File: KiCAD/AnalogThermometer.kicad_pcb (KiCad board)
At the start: 2 copper layers, 26.7 x 25.4 mm, 19 parts, among them P1 Power, P2 uA, Q1 MMBT3904, U1 LTC1541, U2 MCP9700A, U3 MCP9700AT

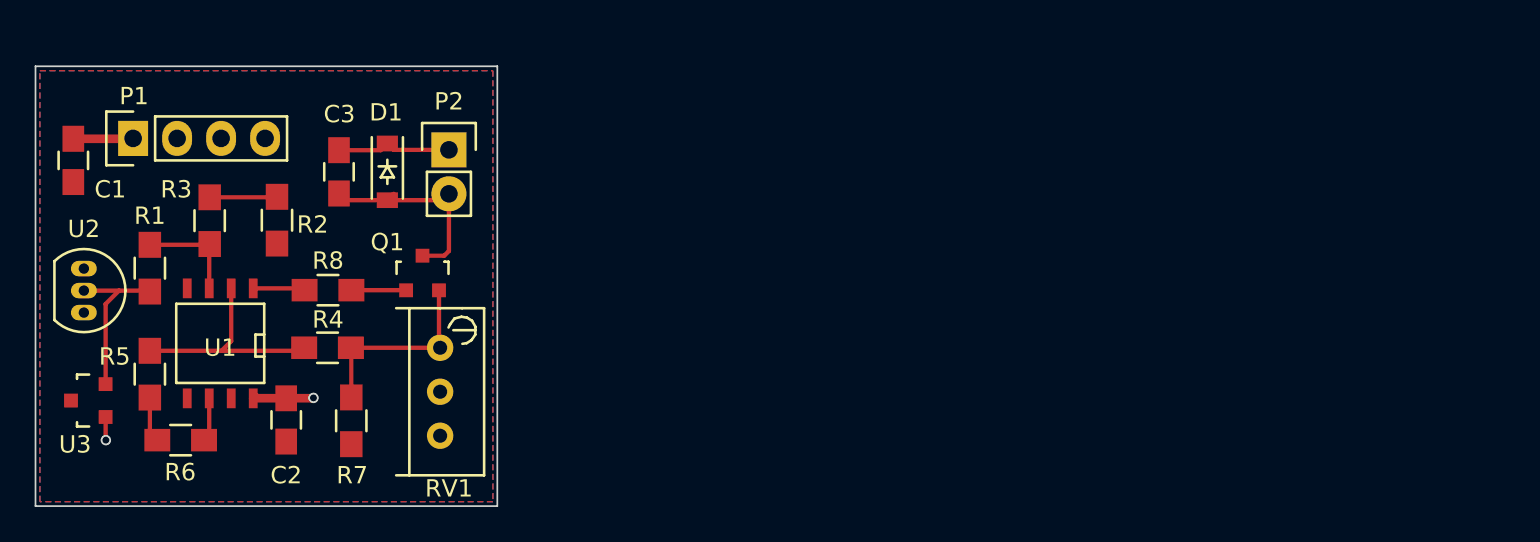
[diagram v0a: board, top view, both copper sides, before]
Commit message: Updated board and gerbers to be 1x1 inch
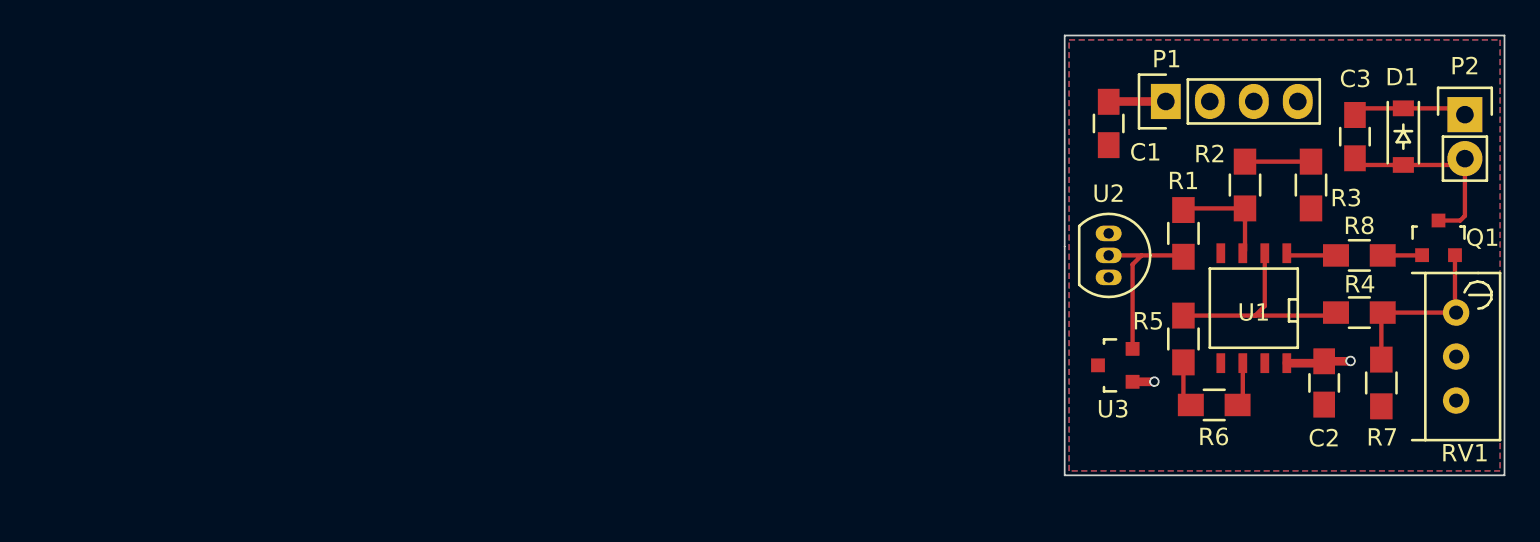
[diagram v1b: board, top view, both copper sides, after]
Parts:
- moved C2 60.0 mm to (132.6, 110.2)
- moved C1 59.8 mm to (120.1, 95.2)
- moved R2 59.8 mm to (128.0, 98.8)
- moved R3 59.7 mm to (131.8, 98.8)
- moved R5 59.7 mm to (124.5, 107.7)
- moved R6 59.7 mm to (126.2, 111.5)
- moved U1 59.7 mm to (128.5, 105.9)
- moved R1 59.7 mm to (124.5, 101.6)
- moved P1 59.7 mm to (123.4, 94.0)
- moved R4 59.6 mm to (134.6, 106.2)
- moved R8 59.6 mm to (134.6, 102.9)
- moved R7 59.5 mm to (135.9, 110.2)
- moved U3 59.3 mm to (120.5, 109.2)
- moved U2 59.2 mm to (120.1, 101.6)
- moved C3 58.7 mm to (134.4, 96.0)
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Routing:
- net Net-(Q1-Pad2): track 11.4 -> 10.3 mm
- net Net-(Q1-Pad1): track 3.19 -> 2.31 mm
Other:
- board size 26.7 x 25.4 mm -> 25.4 x 25.4 mm
